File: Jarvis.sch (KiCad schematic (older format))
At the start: 18 parts, among them IC1 ADP1607, IC2 STM32F411CxUx, IC3 MPU-9250, IC4 MAX-7Q, IC5 MS5611-01BA03, IC6 Si4460, J1 CONN_01x02, J2 CONN_01x02, P1 SWD_TC, U1 MICROSD

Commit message: Added External Connectors & STM32F411CxUx with peripherals configured
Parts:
- removed U1: MICROSD, agg:MICROSD_MOLEX_503398-1892, symbol MICROSD
- added C10, C11, C12, C4, C6, C7, C8, C9, C? (x2): 100nF, symbol C_Small
- added C13, C14: CL, symbol C_Small
- added C15, C3: 4.7uF, symbol C_Small
- added C5: 1uF, symbol C_Small
- added J?: PYRO3, symbol CONN_01x02
- added J?: ARM, symbol CONN_01x02
- added J?: PWR, symbol CONN_01x02
- added R3: RL, agg:0603-L, symbol R_Small
- added R? (x5): 47K, Resistors_SMD:R_0603, symbol R
- added U?: MICROSD, agg:MICROSD_MOLEX_503398-1892, symbol MICROSD
- added X?: AA HOLDER, symbol PART
- added Y1: 26MHz, symbol XTAL
- J1: value CONN_01x02 -> PYRO1
- J2: value CONN_01x02 -> PYRO2
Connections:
- net 3v3: now also IC2.1 (VBAT), IC2.24 (VDD), IC2.36 (VDD), IC2.48 (VDD), IC2.9 (VDDA), P1.1 (VDD), C10.1, C11.1, C12.1, C3.1, C4.1, C5.1, C6.1, C7.1, C8.1, C?.1, C?.1, R?.2, R?.2, R?.2, R?.2, R?.2, U?.4 (VDD)
- net GND: now also IC2.23 (VSS), IC2.35 (VSS), IC2.44 (BOOT0), IC2.47 (VSS), IC2.8 (VSSA), IC2.EP (VSS), J1.2, J2.2, P1.5 (GND), C10.2, C11.2, C12.2, C13.1, C14.1, C15.1, C3.2, C4.2, C5.2, C6.2, C7.2, C8.2, C9.2, C?.2, C?.2, J?.2, J?.2, U?.10 (CD_L), U?.6 (VSS), U?.9 (SHIELD)
- net VBATT: now also J?.1, J?.1
- net BEEPER: now reaches IC2.10 (PA0)
- net SPI4_MOSI: now reaches IC2.11 (PA1)
- net USART1_TX: now reaches IC2.12 (PA2)
- net USART1_RX: now reaches IC2.13 (PA3)
- net PYRO1_S: now reaches IC2.14 (PA4)
- net PYRO1_F: now reaches IC2.15 (PA5)
- net SDIO_CMD: now reaches IC2.16 (PA6)
- net SDIO_CMD: now also R?.1, U?.3 (CMD)
- net SPI5_SCK: now reaches IC2.18 (PB0)
- net SPI5_NSS1: now reaches IC2.19 (PB1)
- net STAT_HBT: now reaches IC2.2 (PC13)
- net PYRO2_S: now reaches IC2.20 (PB2)
- net at IC2.22 (VCAP1): now also C15.2
- net SPI4_NSS1: now reaches IC2.25 (PB12)
- net SPI4_SCK: now reaches IC2.26 (PB13)
- net SD_CD: now reaches IC2.27 (PB14)
- net SD_CD: now also U?.11 (CD_S)
- net SDIO_CK: now reaches IC2.28 (PB15)
- net SDIO_CK: now also U?.5 (CLK)
- net SDIO_D1: now reaches IC2.29 (PA8)
- net SDIO_D1: now also R?.1, U?.8 (DAT1)
- net STAT_ERR: now reaches IC2.3 (PC14)
- net SDIO_D2: now reaches IC2.30 (PA9)
- net SDIO_D2: now also R?.1, U?.1 (DAT2)
- net SPI5_MOSI: now reaches IC2.31 (PA10)
- net SPI4_MISO: now reaches IC2.32 (PA11)
- net SPI5_MISO: now reaches IC2.33 (PA12)
- net SWDIO: now reaches IC2.34 (PA13)
- net SWDIO: now also P1.2 (SWDIO)
- net SWCLK: now reaches IC2.37 (PA14)
- net SWCLK: now also P1.4 (SWDCLK)
- net PYRO2_F: now reaches IC2.39 (PB3)
- net STAT_WRN: now reaches IC2.4 (PC15)
- net SDIO_D0: now reaches IC2.40 (PB4)
- net SDIO_D0: now also R?.1, U?.7 (DAT0)
- net SDIO_D3: now reaches IC2.41 (PB5)
- net SDIO_D3: now also R?.1, U?.2 (DAT3)
- net PYRO3_S: now reaches IC2.42 (PB6)
- net PYRO3_F: now reaches IC2.43 (PB7)
- net I2C1_SCL: now reaches IC2.45 (PB8)
- net I2C1_SDA: now reaches IC2.46 (PB9)
- net at IC2.5 (PH0): now also C13.2, Y1.2
- net at IC2.6 (PH1): now also R3.2
- net ~RST: now reaches IC2.7 (NRST)
- net ~RST: now also P1.3 (~RST), C9.1
- net PYRO1: now reaches J1.1
- net PYRO2: now reaches J2.1
- new net: C14.2, R3.1, Y1.1
- new net PYRO3: J?.1
- new net PYRO_SO: J?.2
- no-connect marks 0 -> 4
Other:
- note added: "COMPONENT SELECTION"
- note added: "External Connectors:"
- note added: "Flight Computer:"
- note added: "GPS on USART1 - MPU9250 on SPI5\nSi4460 on SPI4 - Barometer on I2C1\nSD Card on SDIO"
- note added: "NB. Camera will have its\nown external 5v Supply."
- note added: "Notes:"
- moved on the sheet: AE1, AE2, IC2, IC3, IC4, IC5, IC6, J1, J2, LS1, P1

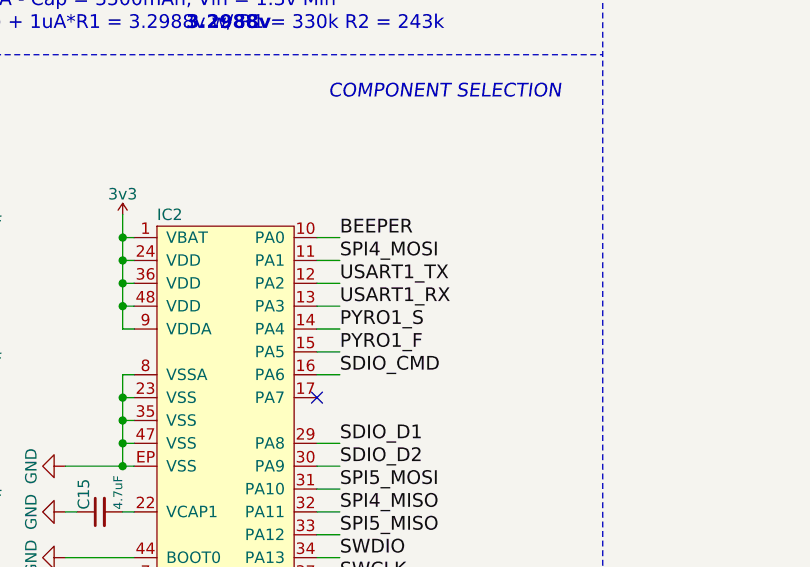
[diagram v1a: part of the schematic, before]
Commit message: Updated ReadMe
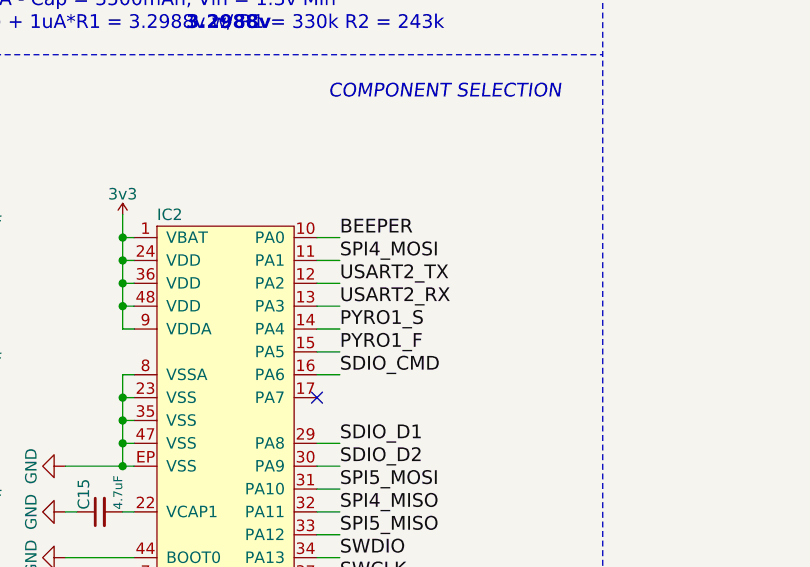
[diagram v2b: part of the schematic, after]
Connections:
- net USART1_RX renamed USART2_RX
- net USART1_TX renamed USART2_TX
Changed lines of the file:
@@
 SD_CD
 Text Label 3100 3700 0    60   ~ 0
-USART1_TX
+USART2_TX
 Text Label 3100 3800 0    60   ~ 0
-USART1_RX
+USART2_RX
 Text Label 3100 6300 0    60   ~ 0
 I2C1_SDA

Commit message: Added Radio & Barometer
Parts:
- removed AE1: ANT, symbol ANT
- added C18: 100pF, symbol C_Small
- added C19: 220pF, symbol C_Small
- added C20, C27, C29: 100nF, symbol C_Small
- added C21: 5.1pF, symbol C_Small
- added C22: 2.7pF, symbol C_Small
- added C23: 18pF, symbol C_Small
- added C24: 8.2pF, symbol C_Small
- added C25: 15pF, symbol C_Small
- added C26: 8.2nF, symbol C_Small
- added C28: 2.2uF, symbol C_Small
- added D1, D2, D3, D4: LED, symbol LED
- added J6: LED_HBT, symbol CONN_01x02
- added J7: LED_ARM, symbol CONN_01x02
- added L2: 56nH, Inductors_NEOSID:Neosid_Inductor_SM-NE29_SMD1008, symbol L_Small
- added L3: 220nH, Inductors_NEOSID:Neosid_Inductor_SM-NE29_SMD1008, symbol L_Small
- added L4, L5: 56nH, symbol L_Small
- added L6, L7: 18nH, Inductors_NEOSID:Neosid_Inductor_SM-NE29_SMD1008, symbol L_Small
- added P2: SMA, symbol SMA
- added R10, R11, R12, R13, R14, R9: R, agg:0603-L, symbol R_Small
- added R15, R16: 10k, agg:0603-L, symbol R_Small
- added X2: 3mm LEDs, symbol PART
- added X3: 433MHz ANT, symbol PART
- added X4: ARM Switch, symbol PART
- added Y2: 30MHz, agg:XTAL-20x16, symbol SMD_XTAL
- C13: footprint (none) -> ~
- gave numbers to parts that had none: 12
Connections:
- net STAT_ERR is gone; now on net STAT_HBT: IC2.3 (PC14)
- net 3v3: now also IC5.1 (VDD), IC5.2 (PS), IC6.6 (VDD), IC6.8 (VDD), C18.1, C19.1, C20.1, C27.1, C28.1, C29.1, L3.2, R15.1, R16.1, R9.1
- net GND: now also IC5.3 (GND), IC5.4 (CSB), IC5.5 (CSB), IC6.1 (SDN), IC6.18 (GND), IC6.5 (NC), IC6.EP (GND), C18.2, C19.2, C20.2, C21.1, C24.2, C25.2, C26.2, C27.2, C28.2, C29.2, D1.1 (K), D2.1 (K), D3.1 (K), D4.1 (K), J6.2, J7.2, P2.2 (GND), P2.3 (GND), P2.4 (GND), P2.5 (GND), Y2.2, Y2.4
- net I2C1_SCL: now also IC5.8 (SCLK), R15.2
- net I2C1_SDA: now also IC5.7 (SDI), R16.2
- net PYRO_SO: now also R14.1
- net SPI4_MISO: now also IC6.13 (SDO)
- net SPI4_MOSI: now also IC6.14 (SDI)
- net SPI4_NSS1: now also IC6.15 (nSEL)
- net SPI4_SCK: now also IC6.12 (SCLK)
- net STAT_HBT: now also R11.1; no longer IC2.2 (PC13)
- net STAT_WRN: now also R12.1
- net VBATT: now also R10.1
- net nIRQ: now reaches IC2.21 (PB10)
- net nIRQ: now also IC6.11 (nIRQ)
- net at IC6.16 (XOUT): now also Y2.1
- net at IC6.17 (XIN): now also Y2.3
- net at IC6.2 (RXp): now also C21.2, L2.2, L4.2
- net at IC6.3 (RXn): now also C22.1, L2.1
- net at IC6.4 (TX): now also C23.1, L3.1
- new net: D1.2 (A), R9.2
- new net: D2.2 (A), R10.2
- new net: D3.2 (A), R11.2
- new net: J7.1, R14.2
- new net: D4.2 (A), R12.2
- new net: J6.1, R13.2
- new net: C25.1, L6.2, L7.1
- new net: C22.2, C24.1, L4.1, L5.2, L6.1
- new net: C26.1, L7.2, P2.1 (RF)
- new net: C23.2, L5.1
- new net STAT_EX_HBT: IC2.2 (PC13), R13.1
- no-connect marks 4 -> 9
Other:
- note added: "- GPS\n- IMU\n- Buzzer\n- Pyro Channels"
- note added: "Barometer:"
- note added: "Datalogging:"
- note added: "Radio:"
- note added: "Status LEDs:"
- note added: "TODO:"
- moved on the sheet: AE2, C10, C11, C12, C13, C14, C15, C16, C17, C3, C4, C5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

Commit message: Progressed Schematic
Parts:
- added C30, C? (x3): 100nF, symbol C_Small
- added C31, C33: 0.1uF, symbol C_Small
- added C32: 10nF, symbol C_Small
- added FB1, FB2: 1.25R, agg:0402-L, symbol R_Small
- added Q1: NFET, agg:SOT-23, symbol NFET
- added Q? (x3): NFET, symbol NFET
- added Q? (x3): PFET, symbol PFET
- added R17, R18, R? (x6): 100R, agg:0603-L, symbol R_Small
- added R19: 0R, agg:0603-L, symbol R_Small
- added R? (x12): 10k, agg:0603-L, symbol R_Small
- added R? (x3): 1R, agg:0603-L, symbol R_Small
- added TP?: TESTPAD, agg:TESTPAD, symbol TESTPAD
- IC4: value MAX-7Q -> MAX-8Q; HabSupplies MAX-7Q -> MAX-8Q
- LS1: footprint (none) -> Library:ABI-042-RC; Farnell (none) -> 1827949
- P2: footprint (none) -> Library:SMA-142-0701-801
- X3: value 433MHz ANT -> 434MHz ANT
- renumbered AE2 to AE1
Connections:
- net 3v3: now also IC3.1 (RESV_VDDIO), IC3.13 (VDD), IC3.8 (VDDIO), IC4.6 (V_BCKP), IC4.7 (VCC_IO), IC4.8 (VCC), LS1.1, C30.1, C31.1, C32.1, R?.1, R?.1, R?.1
- net BEEPER: now also R17.1
- net GND: now also IC3.11 (FSYNC), IC3.18 (GND), IC3.20 (RESV_GND), IC4.1 (GND), IC4.10 (GND), IC4.12 (GND), C30.2, C31.2, C32.2, C33.2, C?.2, C?.2, C?.2, Q1.2 (S), Q?.2 (S), Q?.2 (S), Q?.2 (S), R?.2, R?.2, R?.2
- net PYRO1: now also R?.2, R?.2, R?.2, R?.2
- net PYRO1_F: now also IC2.39 (PB3), R?.1; no longer IC2.15 (PA5)
- net PYRO1_S: now also C?.1, R?.1
- net PYRO2: now also R?.2, R?.2
- net PYRO2_F: now also IC2.42 (PB6), R?.1; no longer IC2.39 (PB3)
- net PYRO2_S: now also IC2.15 (PA5), C?.1, R?.1; no longer IC2.20 (PB2)
- net PYRO3: now also R?.2, R?.2
- net PYRO3_F: now also R?.1
- net PYRO3_S: now also IC2.17 (PA7), C?.1, R?.1; no longer IC2.42 (PB6)
- net PYRO_SO: now also Q?.2 (S), Q?.2 (S), Q?.2 (S), R?.1, R?.1, R?.1
- net SPI5_MISO: now also IC3.9 (AD0/SD0)
- net SPI5_MOSI: now also IC3.24 (SDA/SDI)
- net SPI5_NSS1: now also IC3.22 (~CS)
- net SPI5_SCK: now also IC3.23 (SCL/SCLK)
- net USART2_RX: now also FB1.1
- net USART2_TX: now also FB2.1
- net MPU_IRQ: now reaches IC2.38 (PA15)
- net MPU_IRQ: now also IC3.12 (INT)
- net at IC4.11 (RF_IN): now also AE1.1
- net at IC4.2 (TX): now also FB1.2
- net at IC4.3 (RX): now also FB2.2
- net GPS_RST: now reaches IC4.9 (RESET_N)
- net GPS_RST: now also IC2.20 (PB2)
- net at IC3.10 (REGOUT): now also C33.1
- net at LS1.2: now also R18.1
- net at C26.1, L7.2: now also R19.1; no longer P2.1 (RF)
- new net: P2.1 (RF), R19.2
- new net: Q1.1 (G), R17.2
- new net: Q1.3 (D), R18.2
- new net: Q?.1 (G), R?.1, R?.2 (x3)
- new net: Q?.3 (D), R?.1 (x6)
- new net: Q?.1 (G), R?.2, R?.2 (x3)
- no-connect marks 9 -> 15
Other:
- note added: "150 Hours"
- note added: "18.6 mA"
- note added: "75R"
- note added: "Alarm:"
- note added: "Ferrite Bead for\nEMI Suppresion"
- note added: "Fire"
- note added: "GPS:"
- note added: "IMU:"
- note added: "Id = 3.3v / (75 + 100 + 2.8) = 18.6 mA \nPower = 3.3v * 18.6 mA = 61 mW\n18.6 mA @ 3000 mAh -> 150 Hours"
- note added: "Pyro Channel 1"
- note added: "Pyro Channel 2"
- note added: "Pyro Channel 3"
- note added: "Pyro Channels:"
- note added: "Sense"
- note added: "Vgs = 2v\nRds = 2.8R\nId = 300mA"
- note removed: "- GPS\n- IMU\n- Buzzer\n- Pyro Channels"
- note removed: "GPS on USART1 - MPU9250 on SPI5\nSi4460 on SPI4 - Barometer on I2C1\nSD Card on SDIO"
- note removed: "Notes:"
- note removed: "TODO:"
- moved on the sheet: AE1, C18, C19, C20, C21, C22, C23, C24, C25, C26, C28, C29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
